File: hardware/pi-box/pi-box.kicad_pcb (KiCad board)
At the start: 2 copper layers, 65 x 56 mm, 11 parts, among them J1 Raspberry_Pi_4, J2 RJ45, J3 RJ45

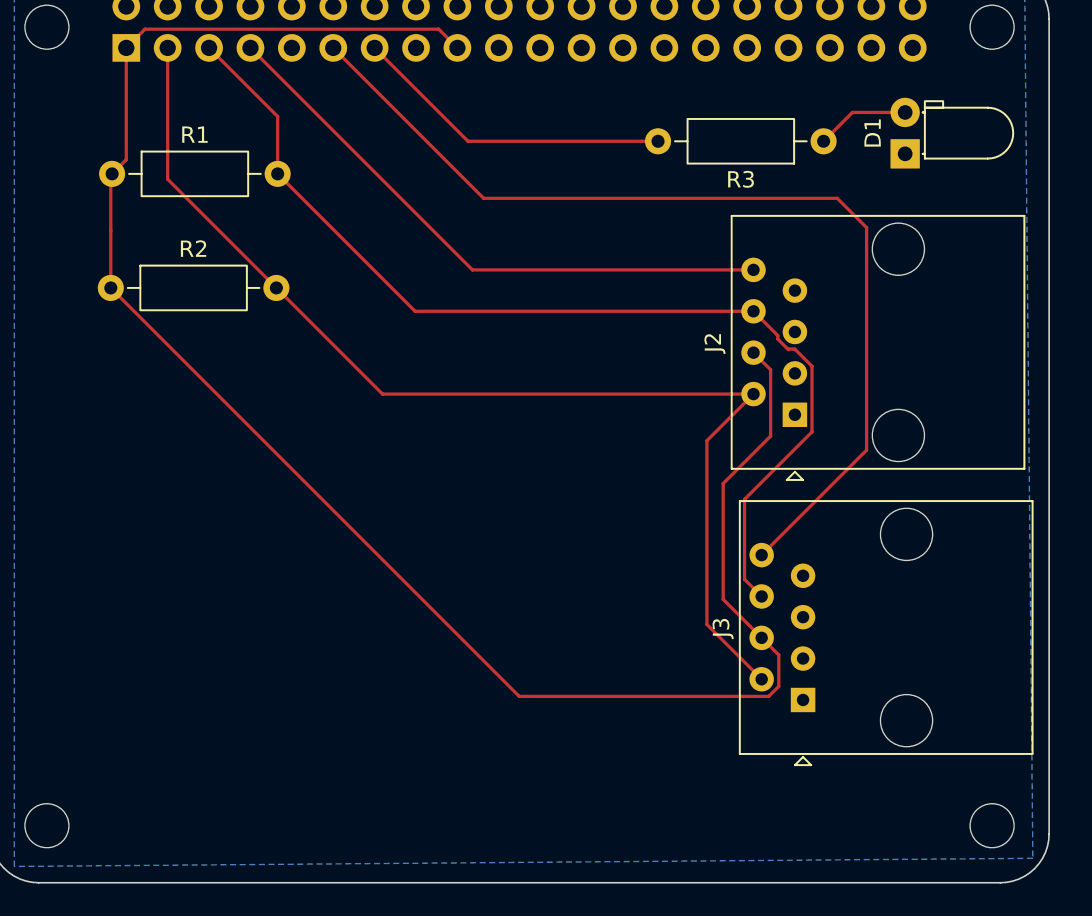
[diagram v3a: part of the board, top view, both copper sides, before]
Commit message: Commit the board state the v1 gerbers were plotted from
The fab outputs went in a commit earlier while the board file still had
uncommitted changes, so fab/v1 corresponded to no committed source at all.
That defeats the only reason to keep gerbers in the repo: being able to look
at a physical board and find exactly what produced it.

Mostly a zone refill, which rewrites every fill polygon coordinate, plus the
plot settings saved into the project file so the next export is one click and
the fab configuration is version-controlled rather than reconstructed.

Co-Authored-By: Claude Opus 5 <noreply@anthropic.com>
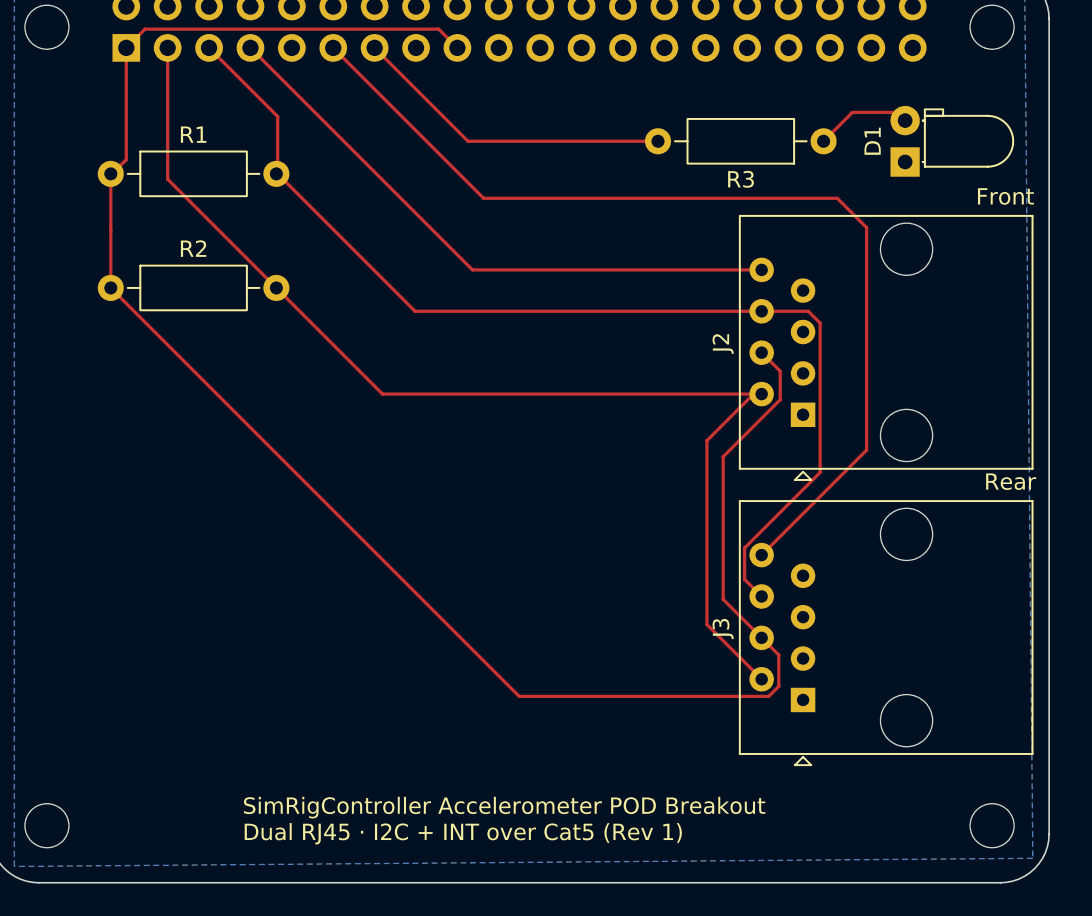
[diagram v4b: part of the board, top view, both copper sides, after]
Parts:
- moved D1 0.50 mm to (80.2, 57.8)
- moved J2 0.50 mm to (73.9, 73.3)
- moved R1 0.08 mm to (31.4, 58.5)
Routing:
- net /SCL: track 63.6 -> 65.2 mm
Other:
- board text added: "Front"
- board text added: "Rear"
- board text added: "SimRigController Accelerometer POD Breakout Dual RJ45 · I2C + INT over Cat5 (Rev 1)"
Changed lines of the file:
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@@
 		(grid_origin 100 100)
 		(pcbplotparams
-			(layerselection 0x00000000_00000000_00000000_000000a5)
+			(layerselection 0x00000000_00000000_55555555_555555f5)
 			(plot_on_all_layers_selection 0x00000000_00000000_00000000_00000000)
 			(disableapertmacros no)
@@
 			(outputformat 1)
 			(mirror no)
-			(drillshape 1)
+			(drillshape 0)
 			(scaleselection 1)
 			(outputdirectory "")
@@
 	(footprint "Connector_RJ:RJ45_Amphenol_54602-x08_Horizontal"
 		(layer "F.Cu")
-		(at 73.4 73.2825 90)
+		(at 73.9 73.2825 90)
 		(descr "8 Pol Shallow Latch Connector, Modjack, RJ45 (https://cdn.amphenol-icc.com/media/wysiwyg/files/drawing/c-bmj-0102.pdf)")
 		(tags "RJ45")
@@
 	(footprint "LED_THT:LED_D3.0mm_Horizontal_O1.27mm_Z10.0mm"
 		(layer "F.Cu")
-		(at 80.165 57.27 90)
+		(at 80.165 57.77 90)
 		(descr "LED, diameter 3.0mm, horizontal offset 1.27mm, z-position of LED center 10.0mm, 2 pins, generated by kicad-footprint-generator")
 		(tags "LED")
@@
 		)
 		(point
-			(at 80.165 56)
+			(at 80.165 56.5)
 			(size 2)
 			(layer "F.Fab")
 		)
 		(point
-			(at 85.235 56)
+			(at 85.235 56.5)
 			(size 2)
 			(layer "F.Fab")
@@
 	(footprint "Resistor_THT:R_Axial_DIN0207_L6.3mm_D2.5mm_P10.16mm_Horizontal"
 		(layer "F.Cu")
-		(at 31.5 58.5)
+		(at 31.42 58.5)
 		(descr "Resistor, Axial_DIN0207 series, Axial, Horizontal, pin pitch=10.16mm, 0.25W = 1/4W, length*diameter=6.3*2.5mm^2, http://cdn-reichelt.de/documents/datenblatt/B400/1_4W%23YAG.pdf")
 		(tags "Resistor Axial_DIN0207 series Axial Horizontal pin pitch 10.16mm 0.25W = 1/4W length 6.3mm diameter 2.5mm")
@@
 		(layer "Edge.Cuts")
 	)
+	(gr_text "SimRigController Accelerometer POD Breakout\nDual RJ45 · I2C + INT over Cat5 (Rev 1)\n"
+		(at 39.5 99.5 0)
+		(layer "F.SilkS")
+		(effects
+			(font
+				(size 1 1)
+				(thickness 0.1)
+			)
+			(justify left bottom)
+		)
+	)
+	(gr_text "Front"
+		(at 84.5 60.5 0)
+		(layer "F.SilkS")
+		(effects
+			(font
+				(size 1 1)
+				(thickness 0.1)
+			)
+			(justify left bottom)
+		)
+	)
+	(gr_text "Rear"
+		(at 85 78 0)
+		(layer "F.SilkS")
+		(effects
+			(font
+				(size 1 1)
+				(thickness 0.1)
+			)
+			(justify left bottom)
+		)
+	)
 	(gr_text "RJ45"
 		(at 100.2 91.84 0)
@@
 	)
 	(segment
-		(start 72.35 68.4225)
-		(end 70.86 66.9325)
+		(start 74.22 66.9325)
+		(end 71.36 66.9325)
 		(width 0.2)
 		(layer "F.Cu")
@@
 	)
 	(segment
-		(start 73.394925 69.2525)
-		(end 72.965075 69.2525)
+		(start 41.66 58.5)
+		(end 41.66 54.98)
 		(width 0.2)
 		(layer "F.Cu")
@@
 	)
 	(segment
-		(start 72.965075 69.2525)
-		(end 72.35 68.637425)
+		(start 70.31 83.3825)
+		(end 70.31 81.457575)
 		(width 0.2)
 		(layer "F.Cu")
@@
 	)
 	(segment
-		(start 70.31 78.4725)
-		(end 74.45 74.3325)
-		(width 0.2)
-		(layer "F.Cu")
-		(net "/SCL")
-	)
-	(segment
-		(start 70.31 83.3825)
-		(end 70.31 78.4725)
+		(start 71.36 84.4325)
+		(end 70.31 83.3825)
 		(width 0.2)
 		(layer "F.Cu")
@@
 	)
 	(segment
-		(start 74.45 70.307575)
-		(end 73.394925 69.2525)
-		(width 0.2)
-		(layer "F.Cu")
-		(net "/SCL")
-	)
-	(segment
-		(start 74.45 74.3325)
-		(end 74.45 70.307575)
-		(width 0.2)
-		(layer "F.Cu")
-		(net "/SCL")
-	)
-	(segment
-		(start 41.66 58.5)
-		(end 41.66 54.98)
-		(width 0.2)
-		(layer "F.Cu")
-		(net "/SCL")
-	)
-	(segment
-		(start 72.35 68.637425)
-		(end 72.35 68.4225)
+		(start 74.95 76.817575)
+		(end 74.95 67.6625)
 		(width 0.2)
 		(layer "F.Cu")
@@
 	)
 	(segment
-		(start 71.36 84.4325)
-		(end 70.31 83.3825)
+		(start 70.31 81.457575)
+		(end 74.95 76.817575)
+		(width 0.2)
+		(layer "F.Cu")
+		(net "/SCL")
+	)
+	(segment
+		(start 74.95 67.6625)
+		(end 74.22 66.9325)
 		(width 0.2)
 		(layer "F.Cu")
@@
 	)
 	(segment
-		(start 69 77.5)
-		(end 69 84.6125)
-		(width 0.2)
-		(layer "F.Cu")
-		(net "+3.3V")
-	)
-	(segment
 		(start 51.54 49.62)
 		(end 52.69 50.77)
@@
 	)
 	(segment
+		(start 72.5 70.6125)
+		(end 71.36 69.4725)
+		(width 0.2)
+		(layer "F.Cu")
+		(net "+3.3V")
+	)
+	(segment
 		(start 31.5 58.5)
 		(end 31.5 59)
@@
 	)
 	(segment
-		(start 71.91 70.5225)
-		(end 71.91 74.59)
-		(width 0.2)
-		(layer "F.Cu")
-		(net "+3.3V")
-	)
-	(segment
-		(start 71.91 74.59)
-		(end 69 77.5)
-		(width 0.2)
-		(layer "F.Cu")
-		(net "+3.3V")
-	)
-	(segment
 		(start 31.5 59)
 		(end 31.42 59.08)
@@
 	)
 	(segment
+		(start 69 75.857425)
+		(end 72.5 72.357425)
+		(width 0.2)
+		(layer "F.Cu")
+		(net "+3.3V")
+	)
+	(segment
 		(start 32.37 57.63)
 		(end 31.5 58.5)
@@
 	)
 	(segment
-		(start 70.86 69.4725)
-		(end 71.91 70.5225)
+		(start 72.5 72.357425)
+		(end 72.5 70.6125)
+		(width 0.2)
+		(layer "F.Cu")
+		(net "+3.3V")
+	)
+	(segment
+		(start 71.36 86.9725)
+		(end 69 84.6125)
 		(width 0.2)
 		(layer "F.Cu")
@@
 	)
 	(segment
-		(start 69 84.6125)
-		(end 71.36 86.9725)
-		(width 0.2)
-		(layer "F.Cu")
-		(net "+3.3V")
-	)
-	(segment
 		(start 72.41 88.0225)
 		(end 71.36 86.9725)
 		(width 0.2)
 		(layer "F.Cu")
+		(net "+3.3V")
+	)
+	(segment
+		(start 69 84.6125)
+		(end 69 75.857425)
+		(width 0.2)
+		(layer "F.Cu")
